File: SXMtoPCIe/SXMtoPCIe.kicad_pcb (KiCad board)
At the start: 4 copper layers, 172.5 x 111.3 mm, 38 parts, among them J1 Bus_PCI_Express_x16, J2 74221-101LF, J3 74221-101LF

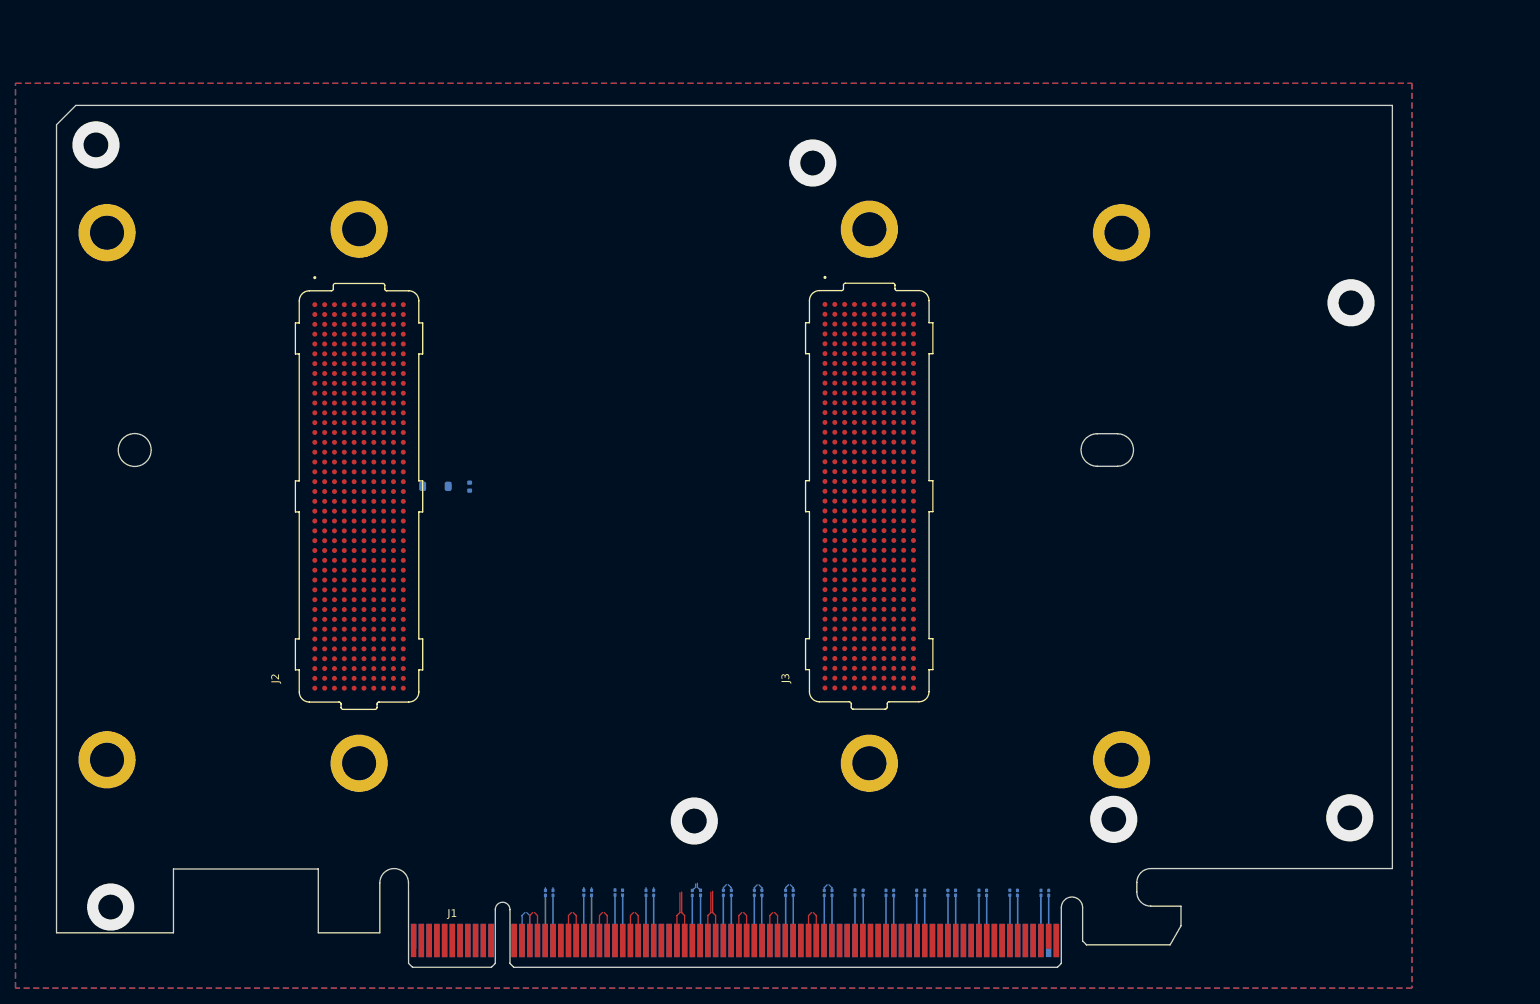
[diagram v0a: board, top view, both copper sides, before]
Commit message: Adds refs, partial routing progress
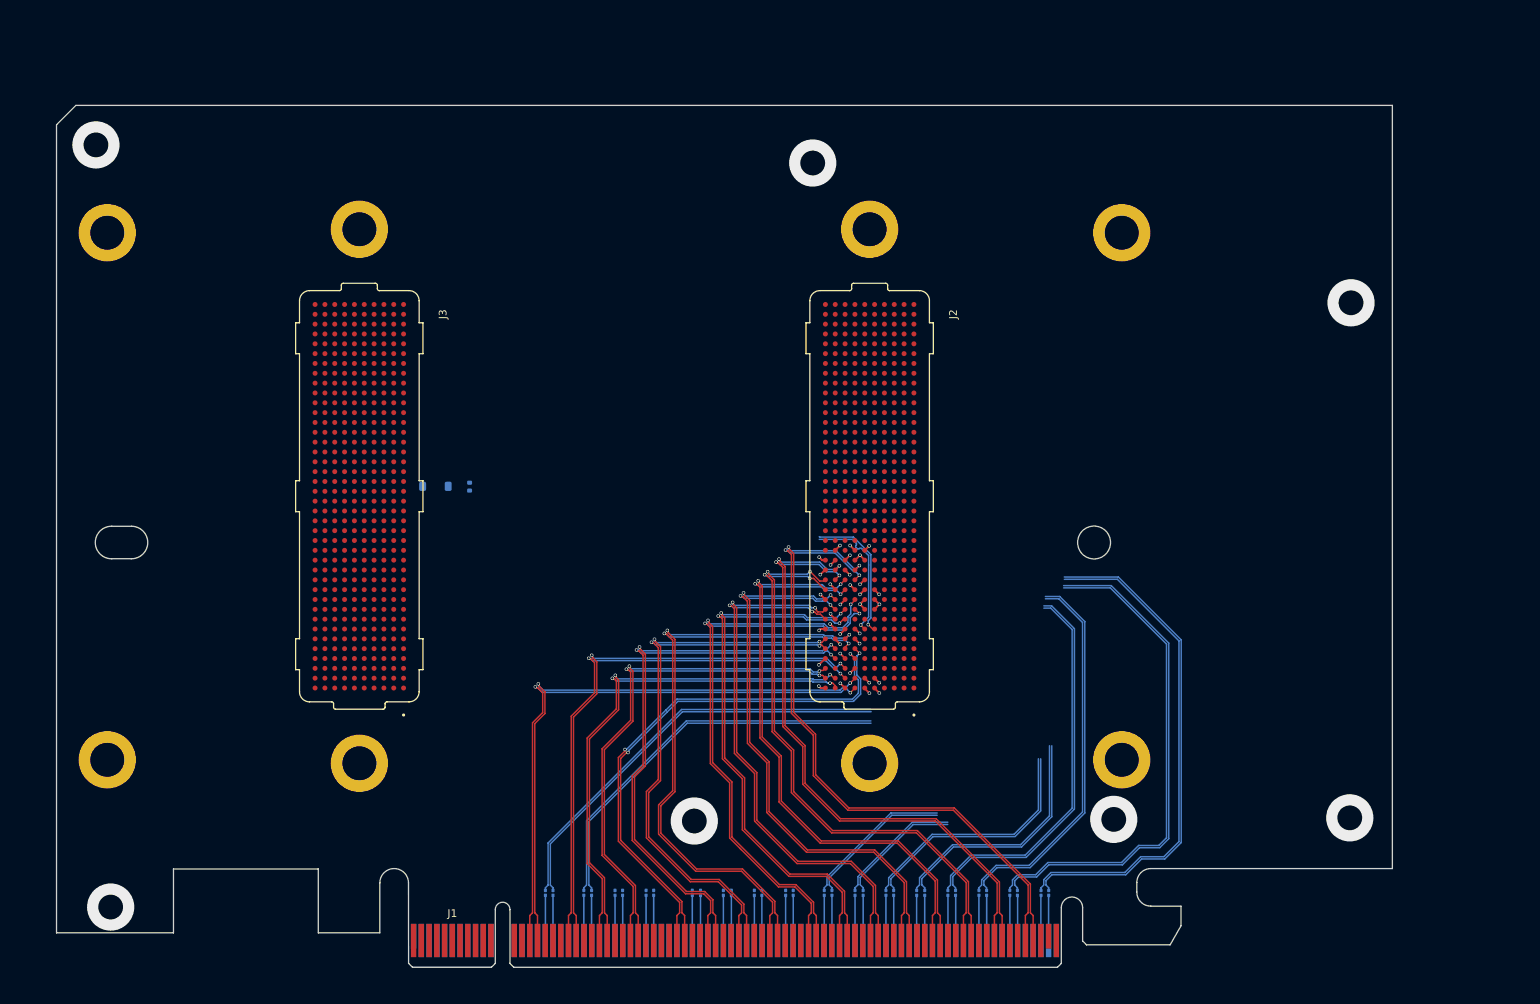
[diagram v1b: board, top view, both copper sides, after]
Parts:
- J2, J3: footprint SXM-AMP:AMPHENOL_74221-101LF -> 74221-101LF:AMPHENOL_74221-101LF
- moved J2 65.9 mm to (173.8, 91.4), turned to -90 degrees
- moved J3 65.8 mm to (107.9, 91.4), turned to -90 degrees
- moved SXMHardware1 4.52 mm to (138.6, 91.4), turned to 180 degrees
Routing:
- net PET15_P: track 0.00 -> 83.3 mm, vias 0 -> 2
- net PET15_N: track 0.00 -> 83.3 mm, vias 0 -> 2
- net PET14_P: track 0.00 -> 77.9 mm, vias 0 -> 2
- net PET14_N: track 0.00 -> 77.9 mm, vias 0 -> 2
- net PET12_P: track 0.00 -> 74.2 mm, vias 0 -> 2
- net PET12_N: track 0.00 -> 74.2 mm, vias 0 -> 2
- net PET13_N: track 0.00 -> 73.3 mm, vias 0 -> 2
- net PET13_P: track 0.00 -> 73.3 mm, vias 0 -> 2
- net PET0_N: track 3.77 -> 76.2 mm, vias 0 -> 2
- net PET0_P: track 3.77 -> 76.2 mm, vias 0 -> 2
- net PET7_P: track 3.77 -> 75.9 mm, vias 0 -> 2
- net PET7_N: track 3.77 -> 75.9 mm, vias 0 -> 2
- net PET11_N: track 0.00 -> 71.6 mm, vias 0 -> 2
- net PET11_P: track 0.00 -> 71.6 mm, vias 0 -> 2
- net PET1_N: track 3.77 -> 72.5 mm, vias 0 -> 2
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- added copper zone on In2.Cu, net (none)
- added copper zone on In1.Cu, net GND
- removed copper zone on B.Cu, net (none)
- removed copper zone on F.Cu, net GND

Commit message: More progress on routing
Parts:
- moved D2 44.7 mm to (162.4, 91.2), turned to 180 degrees
- moved R1 35.9 mm to (158.0, 91.2), turned to 90 degrees
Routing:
- net GND: track 33.3 -> 137.2 mm, vias 34 -> 170
- net REFCLK-: track 17.8 -> 110.5 mm
- net REFCLK+: track 17.9 -> 110.5 mm
- net PER5_P: track 0.00 -> 65.8 mm, vias 0 -> 1
- net PER5_N: track 0.00 -> 65.7 mm, vias 0 -> 1
- net PER6_P: track 0.00 -> 65.1 mm, vias 0 -> 1
- net PER6_N: track 0.00 -> 65.1 mm, vias 0 -> 1
- net PER4_N: track 0.00 -> 63.1 mm, vias 0 -> 1
- net PER4_P: track 0.00 -> 63.1 mm, vias 0 -> 1
- net PER7_N: track 0.00 -> 60.4 mm, vias 0 -> 1
- net PER7_P: track 0.00 -> 60.4 mm, vias 0 -> 1
- net PER15_N: track 65.5 -> 6.57 mm, vias 0 -> 1
- net PER2_P: track 0.00 -> 58.6 mm, vias 0 -> 1
- net PER2_N: track 0.00 -> 58.6 mm, vias 0 -> 1
- net PER15_P: track 65.1 -> 6.61 mm, vias 0 -> 1
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
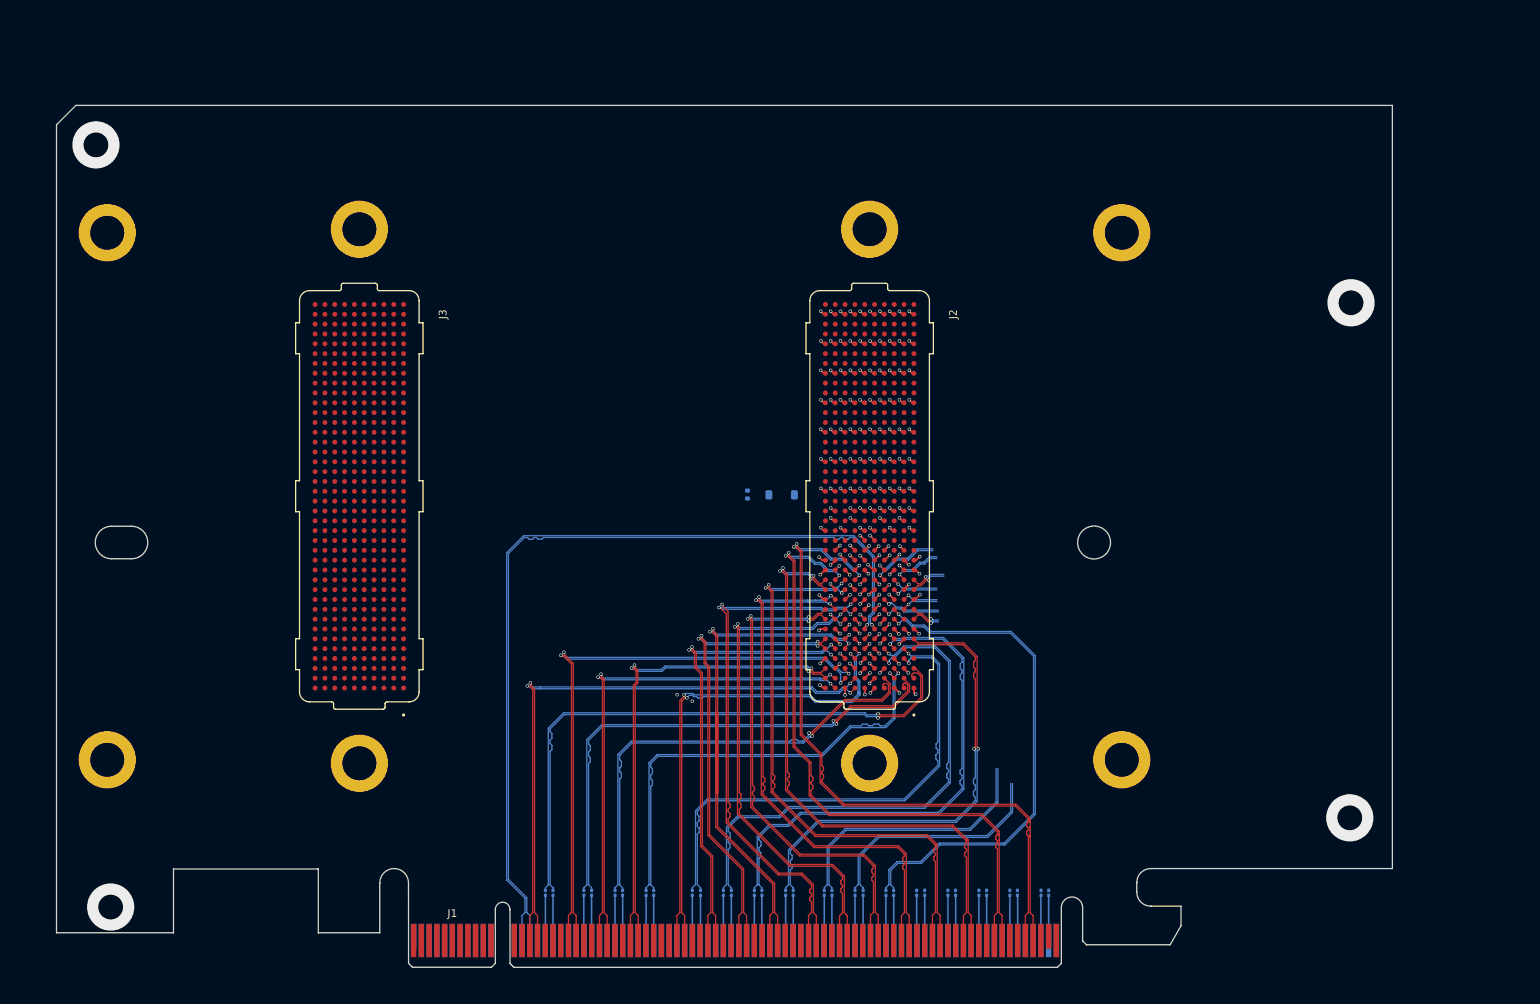
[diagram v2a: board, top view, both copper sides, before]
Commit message: All diff pairs routed
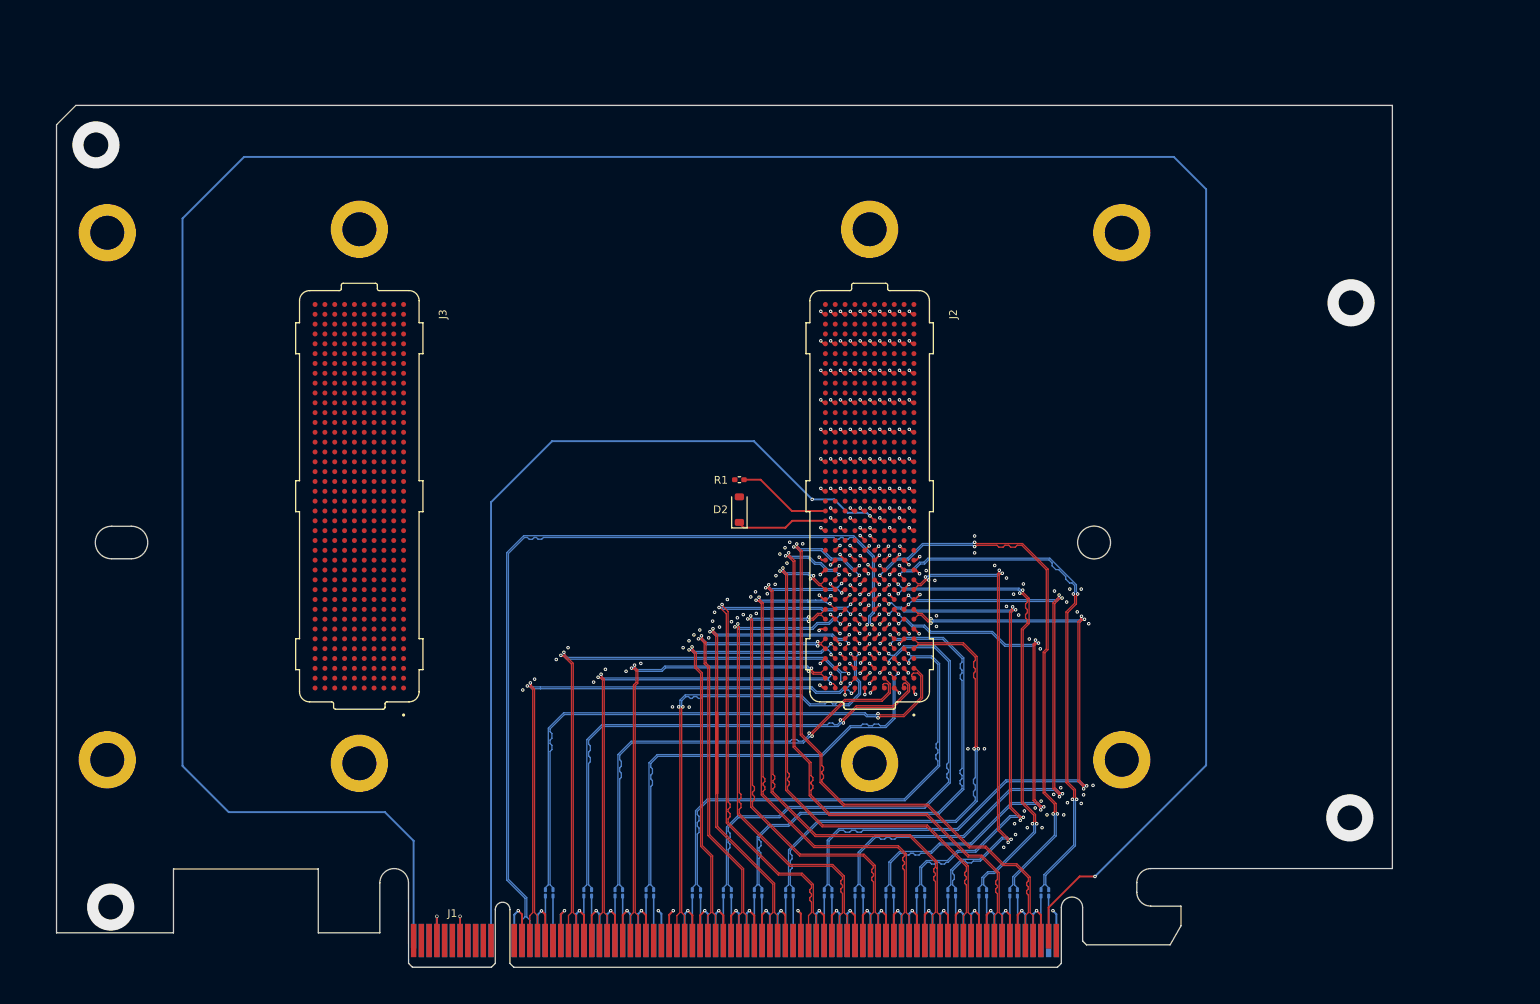
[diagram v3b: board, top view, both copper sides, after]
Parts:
- C1, C10, C11, C12, C13, C14, C15, C16, C17, C18, C19, C2, C20, C21, C22, C23, C24, C25, C26, C27, C28, C29, C3, C30, C31, C32, C4, C5, C6, C7, C8, C9: footprint Capacitor_SMD:C_0201_0603Metric -> Capacitor_SMD:C_0201_0603Metric_Pad0.64x0.40mm_HandSolder
- D2: moved to F.Cu
- R1: footprint Resistor_SMD:R_0402_1005Metric -> Resistor_SMD:R_0402_1005Metric_Pad0.72x0.64mm_HandSolder; moved to F.Cu
- moved D2 5.78 mm to (157.0, 93.1), turned to 90 degrees
- moved R1 2.18 mm to (157.0, 89.3), turned to 180 degrees
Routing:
- net Net-(J1-~{PRSNT1}): track 0.00 -> 360.1 mm, vias 0 -> 1
- net GND: track 137.2 -> 406.3 mm, vias 170 -> 275
- net /PERST: track 0.00 -> 113.7 mm, vias 0 -> 2
- net PER15_N: track 6.57 -> 68.3 mm, vias 1 -> 3
- net PER15_P: track 6.61 -> 68.4 mm, vias 1 -> 3
- net PER14_P: track 9.01 -> 70.5 mm, vias 1 -> 3
- net PER14_N: track 9.01 -> 70.4 mm, vias 1 -> 3
- net PER11_P: track 7.72 -> 65.1 mm, vias 1 -> 3
- net PER11_N: track 7.68 -> 65.1 mm, vias 1 -> 3
- net PER12_P: track 4.73 -> 60.3 mm, vias 1 -> 3
- net PER12_N: track 4.73 -> 60.3 mm, vias 1 -> 3
- net PER13_N: track 5.96 -> 60.8 mm, vias 1 -> 3
- net PER13_P: track 5.92 -> 60.8 mm, vias 1 -> 3
- net PER8_N: track 38.2 -> 89.0 mm, vias 1 -> 3
- net PER8_P: track 38.2 -> 89.0 mm, vias 1 -> 3
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- added copper zone on In2.Cu, net GND
- removed copper zone on In2.Cu, net (none)

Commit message: Power routing more or less complete
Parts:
- added C33: 470uF, Capacitor_SMD:CP_Elec_6.3x7.7, F.Cu at (222.1, 55.6)
- added C34: 470uF, Capacitor_SMD:CP_Elec_6.3x7.7, F.Cu at (222.1, 63.7)
- added C35: 470uF, Capacitor_SMD:CP_Elec_6.3x7.7, F.Cu at (222.1, 71.8)
- added C36: 470uF, Capacitor_SMD:CP_Elec_6.3x7.7, F.Cu at (222.1, 80.0)
- added J4: Molex_45586-0005, 45586-0005:CONN_455860000-SD_MOL, F.Cu at (241.2, 51.8)
- added J5: Molex_45586-0005, 45586-0005:CONN_455860000-SD_MOL, F.Cu at (241.2, 72.1)
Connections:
- net +12V renamed +12VPCI
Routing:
- net Net-(J1-~{PRSNT1}): track 360.1 -> 137.3 mm
- net +12VPCI: track 0.00 -> 99.1 mm, vias 0 -> 211
- net GND: track 406.3 -> 412.8 mm, vias 275 -> 354
- net /PERST: vias 2 -> 1
- added copper zone on F.Cu, net +12VPCI
- added copper zone on In2.Cu, net +12VPCI
- added copper zone on B.Cu, net GND
- added copper zone on F.Cu, net GND
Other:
- board size 172.5 x 111.3 mm -> 187 x 111.3 mm

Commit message: Mounting holes, finishing touches
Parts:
- added H1: Bracket, MountingHole:MountingHole_3.2mm_M3_Pad_Via, F.Cu at (75.0, 47.0)
- added H2: Bracket, MountingHole:MountingHole_3.2mm_M3_Pad_Via, F.Cu at (75.0, 67.0)
- added H3: Bracket, MountingHole:MountingHole_3.2mm_M3_Pad_Via, F.Cu at (75.0, 112.0)
- added H4: Bracket, MountingHole:MountingHole_3.2mm_M3_Pad_Via, F.Cu at (75.0, 142.0)
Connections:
- net Net-(J1-+12V-PadA2) renamed +12V
- J1 pad A10: Net-(J1-+3.3V-PadA10) -> +3V3
- J1 pad A9: Net-(J1-+3.3V-PadA10) -> +3V3
- J1 pad B8: Net-(J1-+3.3V-PadA10) -> +3V3
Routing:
- net +3V3: track 0.00 -> 98.8 mm, vias 0 -> 1
- net Net-(J1-~{PRSNT1}): track 137.3 -> 187.0 mm
- net GND: track 412.8 -> 438.2 mm, vias 354 -> 742
- net +12V: track 0.00 -> 20.6 mm, vias 0 -> 1
- net PET7_P: track 84.0 -> 64.2 mm
- net PET5_N: track 58.8 -> 63.8 mm
- net PET5_P: track 58.8 -> 63.8 mm
- net PET6_N: track 58.6 -> 63.0 mm
- net PET6_P: track 58.6 -> 63.0 mm
- net PET13_N: track 73.3 -> 76.3 mm
- net PET13_P: track 73.2 -> 76.3 mm
- net PET11_P: track 69.6 -> 72.5 mm
- net PET11_N: track 69.7 -> 72.5 mm
- net PET8_P: track 68.7 -> 70.8 mm
- net PET14_P: track 78.8 -> 81.0 mm
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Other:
- outline, holes or cut-outs redrawn
- board text added: "+12V unused"
- board text added: "PCI Mounting Holes #4-40 UNC or M3"
